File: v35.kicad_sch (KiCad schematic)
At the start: 43 parts, among them U10 74ALVC164245, U6 74ALVC164245, U7 74ALVC164245

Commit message: Fab changes
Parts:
- C16, C17: MPN C14663 -> C15849
- R1, R10, R11, R12, R13, R14, R15, R16, R17, R18, R19, R2, R20, R21, R22, R23, R24, R25, R26, R27, R28, R3, R4, R5, R6, R7, R8, R9: MPN (none) -> C25804

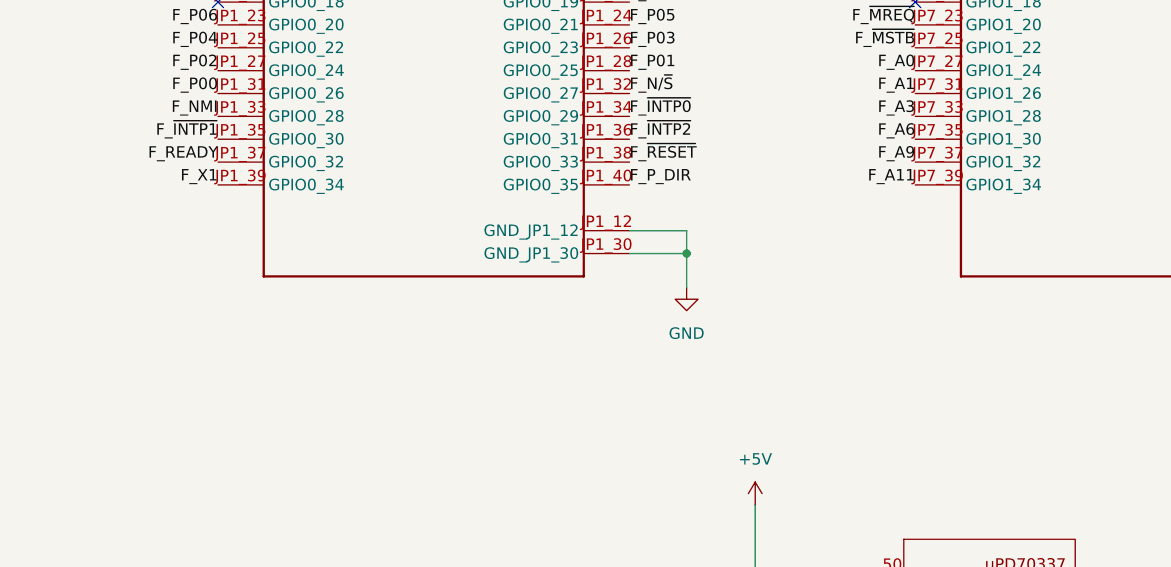
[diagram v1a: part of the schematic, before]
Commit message: Power tweaks. Revision 1 production submitted
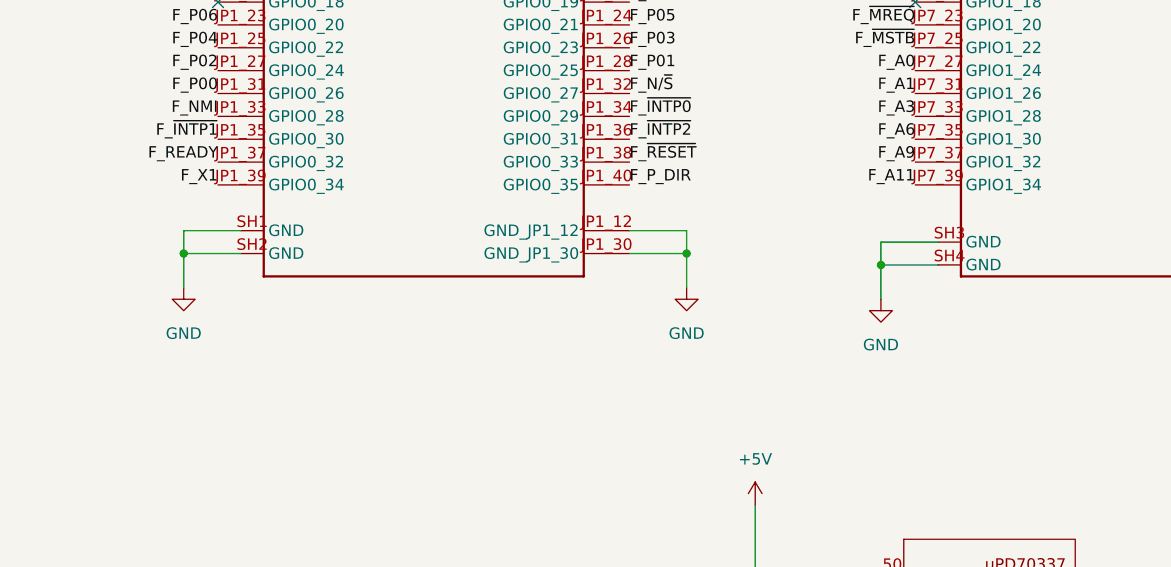
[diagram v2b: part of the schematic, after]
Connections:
- net GND: now also U8.SH1 (GND), U8.SH2 (GND), U8.SH3 (GND), U8.SH4 (GND)
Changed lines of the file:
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@@
 	)
 	(junction
+		(at 342.9 88.9)
+		(diameter 0)
+		(color 0 0 0 0)
+	)
+	(junction
 		(at 31.75 43.18)
 		(diameter 0)
@@
 	)
 	(junction
+		(at 265.43 87.63)
+		(diameter 0)
+		(color 0 0 0 0)
+	)
+	(junction
 		(at 173.99 180.34)
 		(diameter 0)
@@
 	(wire
 		(pts
+			(xy 342.9 86.36) (xy 342.9 88.9)
+		)
+		(stroke
+			(width 0)
+			(type default)
+		)
+	)
+	(wire
+		(pts
 			(xy 173.99 212.09) (xy 173.99 214.63)
 		)
@@
 	(wire
 		(pts
+			(xy 349.25 88.9) (xy 342.9 88.9)
+		)
+		(stroke
+			(width 0)
+			(type default)
+		)
+	)
+	(wire
+		(pts
 			(xy 55.88 80.01) (xy 54.61 80.01)
 		)
@@
 	(wire
 		(pts
+			(xy 265.43 87.63) (xy 265.43 91.44)
+		)
+		(stroke
+			(width 0)
+			(type default)
+		)
+	)
+	(wire
+		(pts
 			(xy 173.99 228.6) (xy 173.99 231.14)
 		)
@@
 	(wire
 		(pts
+			(xy 349.25 86.36) (xy 342.9 86.36)
+		)
+		(stroke
+			(width 0)
+			(type default)
+		)
+	)
+	(wire
+		(pts
 			(xy 173.99 199.39) (xy 173.99 201.93)
 		)
@@
 	(wire
 		(pts
+			(xy 265.43 85.09) (xy 265.43 87.63)
+		)
+		(stroke
+			(width 0)
+			(type default)
+		)
+	)
+	(wire
+		(pts
+			(xy 342.9 88.9) (xy 342.9 92.71)
+		)
+		(stroke
+			(width 0)
+			(type default)
+		)
+	)
+	(wire
+		(pts
 			(xy 173.99 182.88) (xy 173.99 185.42)
 		)
@@
 	(wire
 		(pts
+			(xy 271.78 85.09) (xy 265.43 85.09)
+		)
+		(stroke
+			(width 0)
+			(type default)
+		)
+	)
+	(wire
+		(pts
 			(xy 203.2 29.21) (xy 204.47 29.21)
 		)
@@
 	(wire
 		(pts
+			(xy 271.78 87.63) (xy 265.43 87.63)
+		)
+		(stroke
+			(width 0)
+			(type default)
+		)
+	)
+	(wire
+		(pts
 			(xy 252.73 148.59) (xy 252.73 147.32)
 		)
@@
 	)
 	(symbol
+		(lib_id "power:GND")
+		(at 342.9 92.71 0)
+		(mirror y)
+		(unit 1)
+		(exclude_from_sim no)
+		(in_bom yes)
+		(on_board yes)
+		(dnp no)
+		(fields_autoplaced yes)
+		(property "Reference" "#PWR036"
+			(at 342.9 99.06 0)
+			(effects
+				(font
+					(size 1.27 1.27)
+				)
+				(hide yes)
+			)
+		)
+		(property "Value" "GND"
+			(at 342.9 97.79 0)
+			(effects
+				(font
+					(size 1.27 1.27)
+				)
+			)
+		)
+		(property "Footprint" ""
+			(at 342.9 92.71 0)
+			(effects
+				(font
+					(size 1.27 1.27)
+				)
+				(hide yes)
+			)
+		)
+		(property "Datasheet" ""
+			(at 342.9 92.71 0)
+			(effects
+				(font
+					(size 1.27 1.27)
+				)
+				(hide yes)
+			)
+		)
+		(property "Description" "Power symbol creates a global label with name \"GND\" , ground"
+			(at 342.9 92.71 0)
+			(effects
+				(font
+					(size 1.27 1.27)
+				)
+				(hide yes)
+			)
+		)
+		(pin "1"
+		)
+		(instances
+			(project "NEC-DE10"
+				(path "/ddde7423-f6ec-43a3-9d7f-3b7e70f4bb41/ccac01a1-2c43-4218-b3e2-3fa27929b8d3"
+					(reference "#PWR036")
+					(unit 1)
+				)
+			)
+		)
+	)
+	(symbol
 		(lib_id "power:+3.3V")
 		(at 20.32 22.86 0)
@@
 		(pin "JP1_17"
 		)
+		(pin "SH1"
+		)
+		(pin "SH2"
+		)
+		(pin "SH3"
+		)
+		(pin "SH4"
+		)
 		(instances
 			(project "NEC-DE10"
@@
 	)
 	(symbol
+		(lib_id "power:GND")
+		(at 265.43 91.44 0)
+		(mirror y)
+		(unit 1)
+		(exclude_from_sim no)
+		(in_bom yes)
+		(on_board yes)
+		(dnp no)
+		(fields_autoplaced yes)
+		(property "Reference" "#PWR034"
+			(at 265.43 97.79 0)
+			(effects
+				(font
+					(size 1.27 1.27)
+				)
+				(hide yes)
+			)
+		)
+		(property "Value" "GND"
+			(at 265.43 96.52 0)
+			(effects
+				(font
+					(size 1.27 1.27)
+				)
+			)
+		)
+		(property "Footprint" ""
+			(at 265.43 91.44 0)
+			(effects
+				(font
+					(size 1.27 1.27)
+				)
+				(hide yes)
+			)
+		)
+		(property "Datasheet" ""
+			(at 265.43 91.44 0)
+			(effects
+				(font
+					(size 1.27 1.27)
+				)
+				(hide yes)
+			)
+		)
+		(property "Description" "Power symbol creates a global label with name \"GND\" , ground"
+			(at 265.43 91.44 0)
+			(effects
+				(font
+					(size 1.27 1.27)
+				)
+				(hide yes)
+			)
+		)
+		(pin "1"
+		)
+		(instances
+			(project "NEC-DE10"
+				(path "/ddde7423-f6ec-43a3-9d7f-3b7e70f4bb41/ccac01a1-2c43-4218-b3e2-3fa27929b8d3"
+					(reference "#PWR034")
+					(unit 1)
+				)
+			)
+		)
+	)
+	(symbol
 		(lib_id "Device:C_Small")
 		(at 88.9 40.64 0)
@@
 	)
 	(symbol
+		(lib_name "P0496_1")
 		(lib_id "NEC-DE10:P0496")
 		(at 292.1 57.15 0)
@@
 		(pin "JP1_17"
 		)
+		(pin "SH1"
+		)
+		(pin "SH2"
+		)
+		(pin "SH3"
+		)
+		(pin "SH4"
+		)
 		(instances

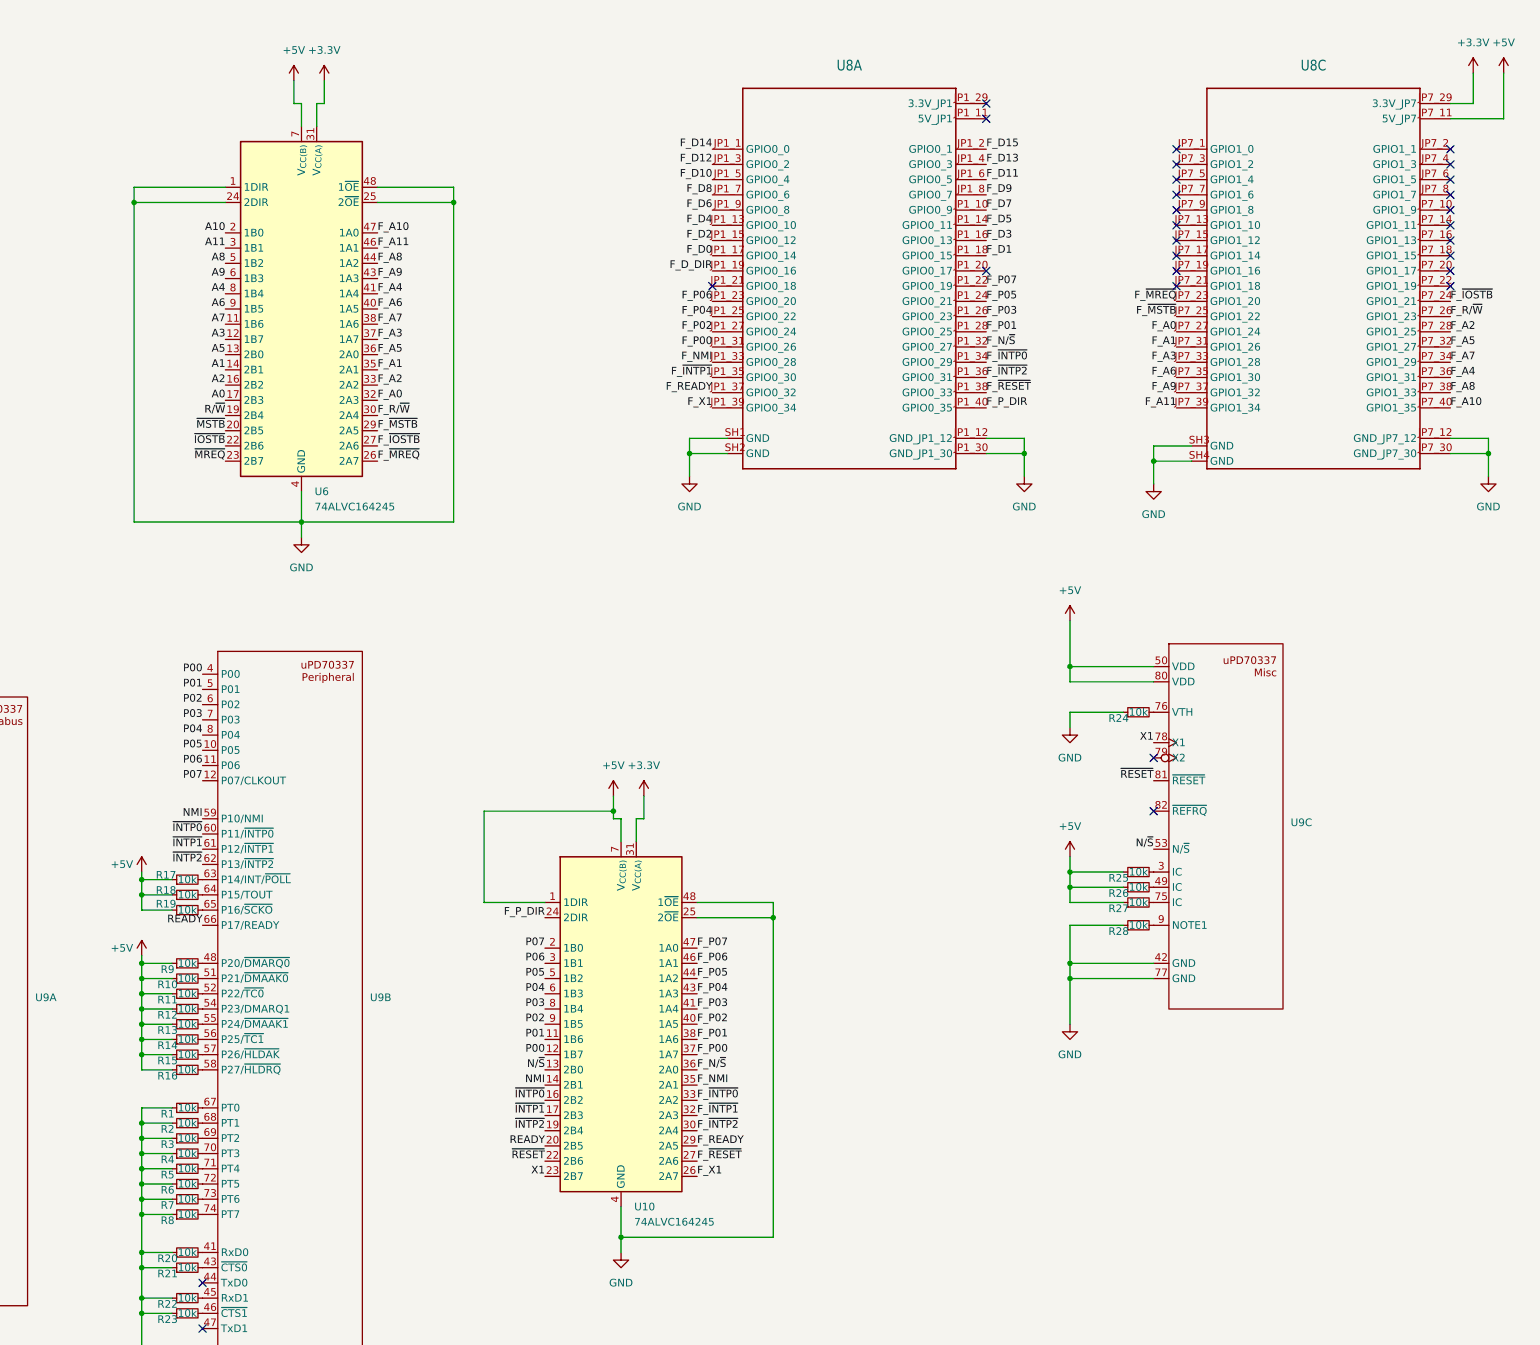
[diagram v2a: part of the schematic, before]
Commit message: Adding power control Moving board around for heat issues
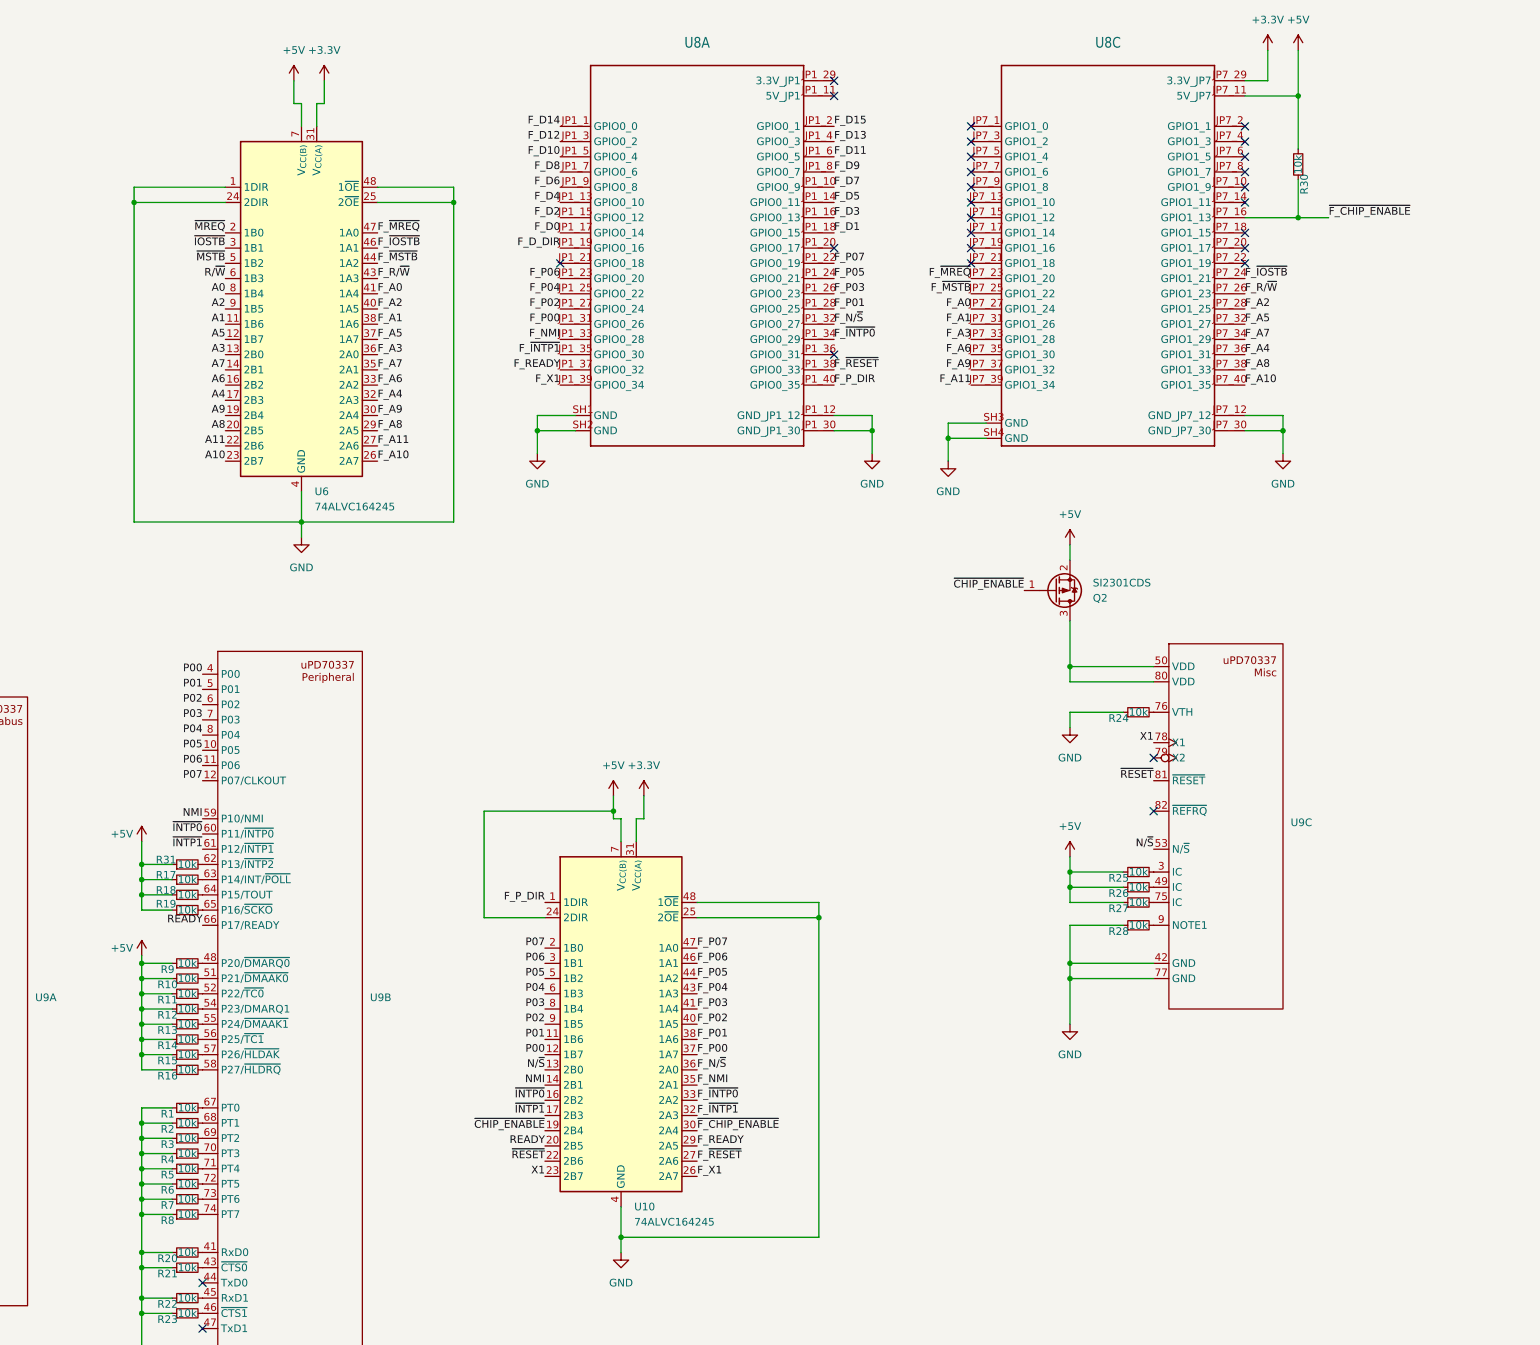
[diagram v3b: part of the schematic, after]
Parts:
- added Q2: SI2301CDS, Package_TO_SOT_SMD:SOT-23, symbol Device:Q_PMOS_GSD
- added R30, R31: 10k, Resistor_SMD:R_0603_1608Metric, symbol Device:R_Small
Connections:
- net +5V: now also U10.24 (2DIR), Q2.2 (S), R30.2, R31.1; no longer U10.1 (1DIR), U9.50 (VDD), U9.80 (VDD)
- net A0: now also U6.8 (1B4); no longer U6.17 (2B3)
- net A1: now also U6.11 (1B6); no longer U6.14 (2B1)
- net A10: now also U6.23 (2B7); no longer U6.2 (1B0)
- net A11: now also U6.22 (2B6); no longer U6.3 (1B1)
- net A2: now also U6.9 (1B5); no longer U6.16 (2B2)
- net A3: now also U6.13 (2B0); no longer U6.12 (1B7)
- net A4: now also U6.17 (2B3); no longer U6.8 (1B4)
- net A5: now also U6.12 (1B7); no longer U6.13 (2B0)
- net A6: now also U6.16 (2B2); no longer U6.9 (1B5)
- net A7: now also U6.14 (2B1); no longer U6.11 (1B6)
- net A8: now also U6.20 (2B5); no longer U6.5 (1B2)
- net A9: now also U6.19 (2B4); no longer U6.6 (1B3)
- net F_A0: now also U6.41 (1A4); no longer U6.32 (2A3)
- net F_A1: now also U6.38 (1A6); no longer U6.35 (2A1)
- net F_A10: now also U6.26 (2A7); no longer U6.47 (1A0)
- net F_A11: now also U6.27 (2A6); no longer U6.46 (1A1)
- net F_A2: now also U6.40 (1A5); no longer U6.33 (2A2)
- net F_A3: now also U6.36 (2A0); no longer U6.37 (1A7)
- net F_A4: now also U6.32 (2A3); no longer U6.41 (1A4)
- net F_A5: now also U6.37 (1A7); no longer U6.36 (2A0)
- net F_A6: now also U6.33 (2A2); no longer U6.40 (1A5)
- net F_A7: now also U6.35 (2A1); no longer U6.38 (1A6)
- net F_A8: now also U6.29 (2A5); no longer U6.44 (1A2)
- net F_A9: now also U6.30 (2A4); no longer U6.43 (1A3)
- net F_P_DIR: now also U10.1 (1DIR); no longer U10.24 (2DIR)
- net F_R/~{W}: now also U6.43 (1A3); no longer U6.30 (2A4)
- net F_~{IOSTB}: now also U6.46 (1A1); no longer U6.27 (2A6)
- net F_~{MREQ}: now also U6.47 (1A0); no longer U6.26 (2A7)
- net F_~{MSTB}: now also U6.44 (1A2); no longer U6.29 (2A5)
- net R/~{W}: now also U6.6 (1B3); no longer U6.19 (2B4)
- net ~{IOSTB}: now also U6.3 (1B1); no longer U6.22 (2B6)
- net ~{MREQ}: now also U6.2 (1B0); no longer U6.23 (2B7)
- net ~{MSTB}: now also U6.5 (1B2); no longer U6.20 (2B5)
- net ~{F_CHIP_ENABLE}: now reaches U8.JP7_16 (GPIO1_13)
- net ~{F_CHIP_ENABLE}: now also U10.30 (2A4), R30.1
- net F_~{INTP2}: no longer names the net of U8.JP1_36 (GPIO0_31)
- net F_~{INTP2}: no longer U10.30 (2A4)
- net ~{INTP2}: no longer names the net of U9.62 (P13/~{INTP2})
- net ~{INTP2}: now also R31.2; no longer U10.19 (2B4)
- new net: Q2.3 (D), U9.50 (VDD), U9.80 (VDD)
- new net ~{CHIP_ENABLE}: Q2.1 (G), U10.19 (2B4)
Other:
- moved on the sheet: U8A, U8C
